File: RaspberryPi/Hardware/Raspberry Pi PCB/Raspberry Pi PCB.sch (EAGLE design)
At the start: 1 part

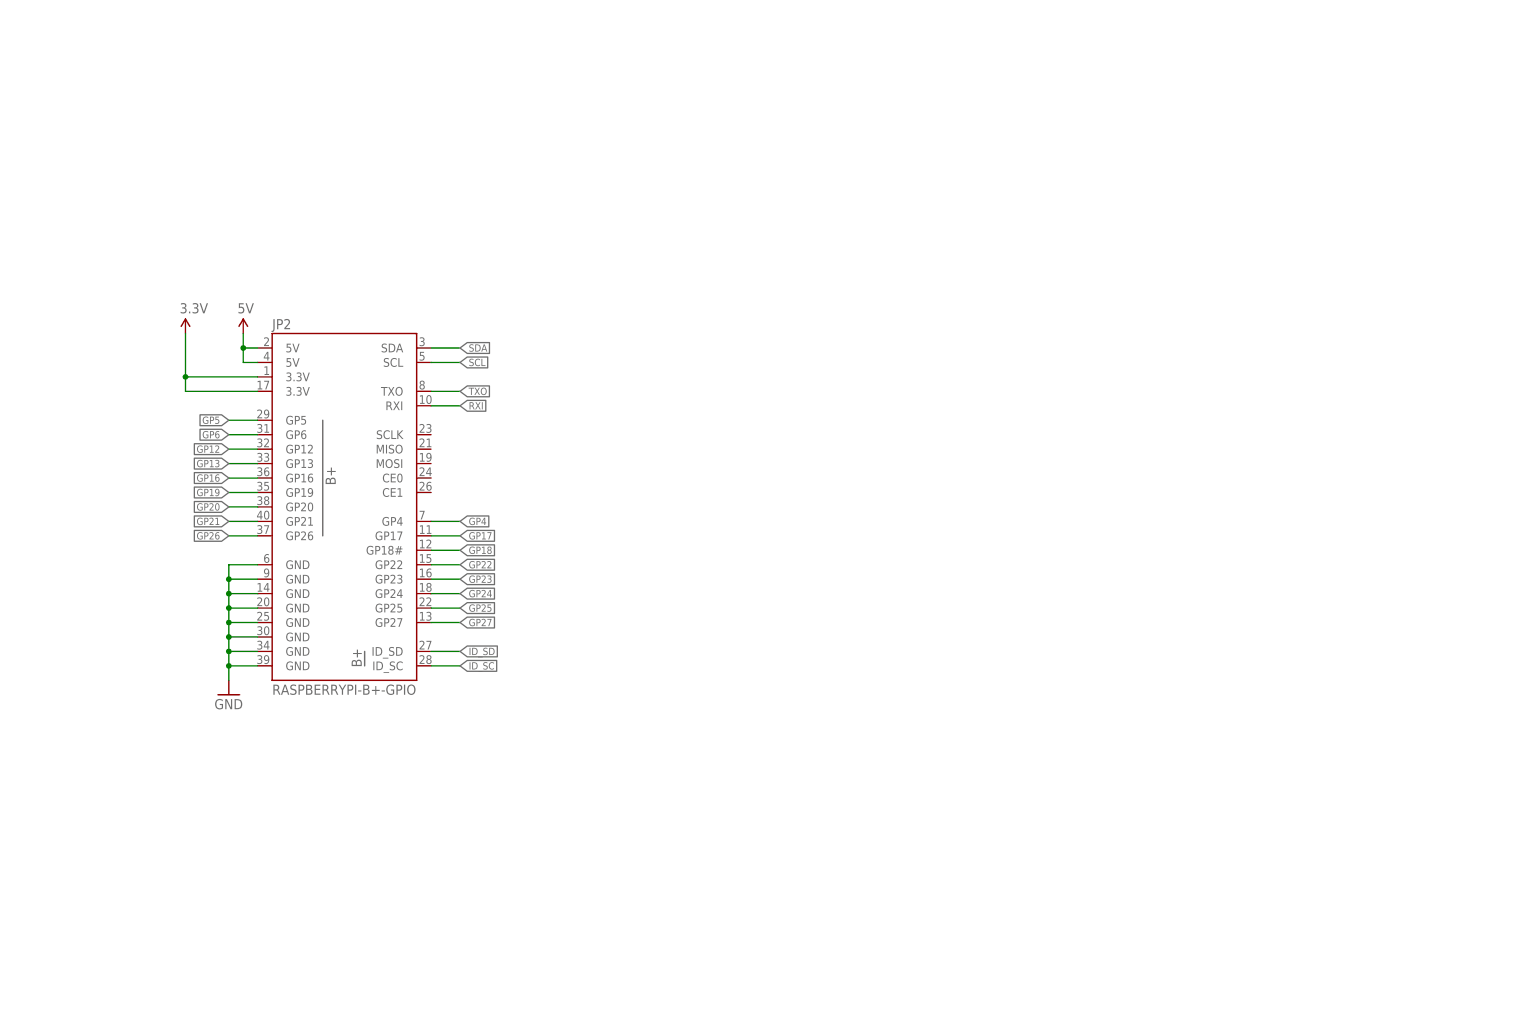
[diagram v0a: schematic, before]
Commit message: Added some necessary components for powering the Raspberry.
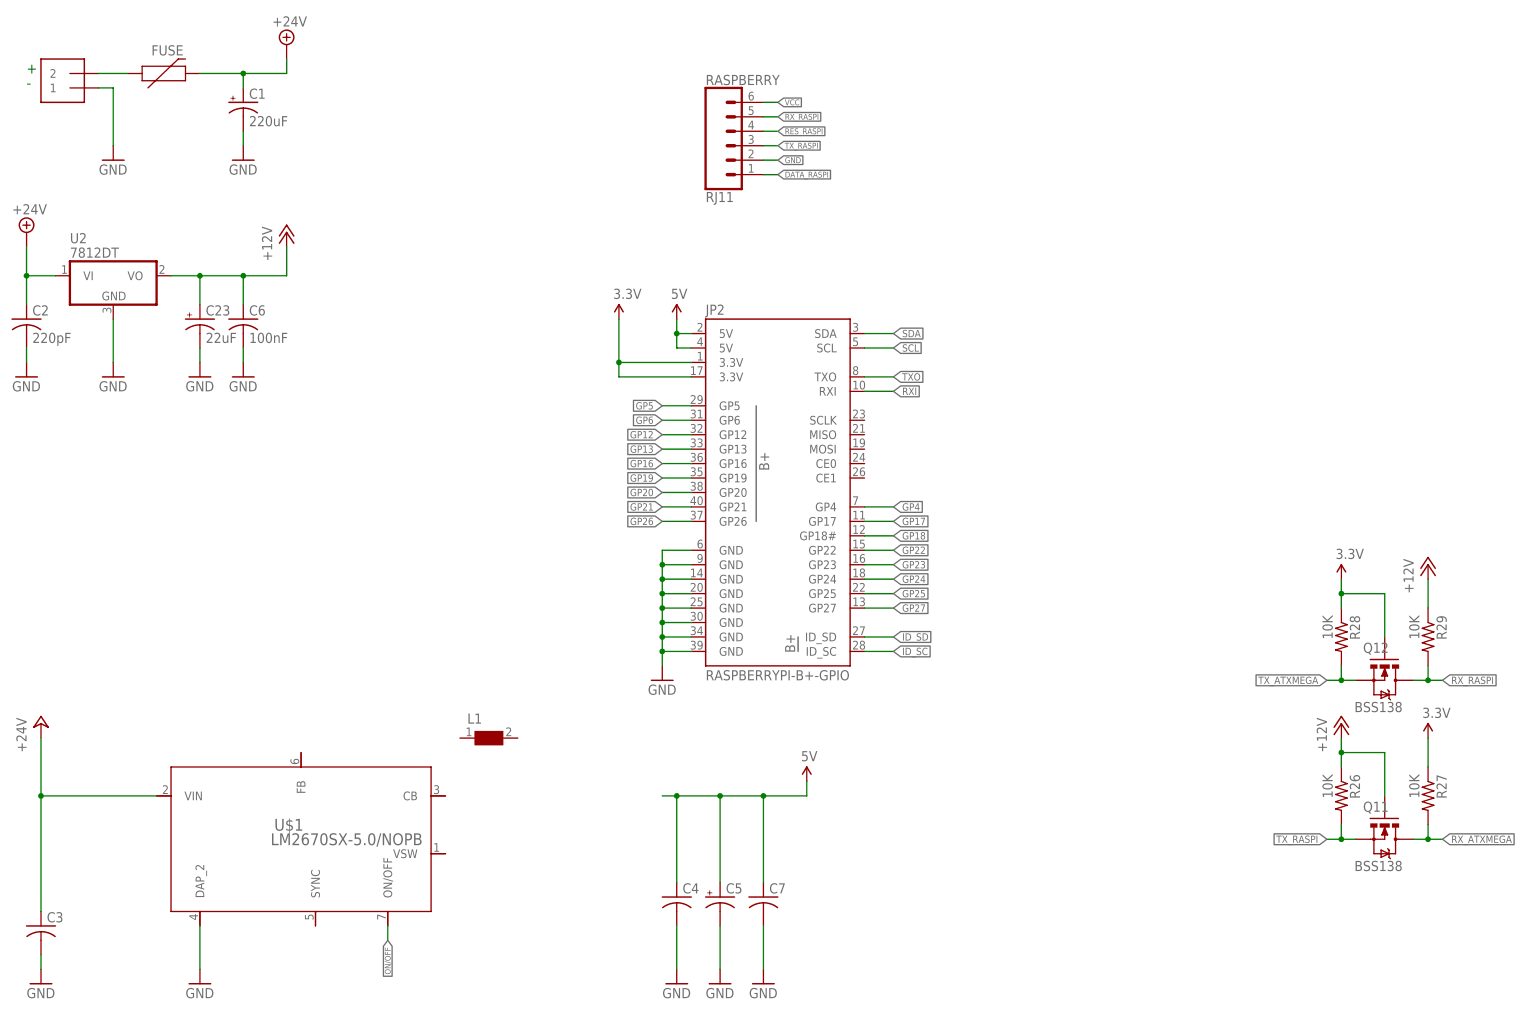
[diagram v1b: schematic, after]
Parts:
- added C1: 220uF, adafruit:CPOL-US175TMP-0810
- added C2: 220pF, adafruit:C-USC1206
- added C23: 22uF, adafruit:CPOL-US153CLV-0505
- added C3: (no value), adafruit:C-USC1206
- added C4, C7: (no value), adafruit:C-USC0805
- added C5: (no value), adafruit:CPOL-US153CLV-0505
- added C6: 100nF, adafruit:C-USC0805
- added FUSE: 6V/0.5A, SparkFun-Fuses:PPTC_HALF-AMP
- added J1: 1X2-3.5MM, adafruit:1X2-3.5MM
- added L1: (no value), WE-PD:WE-PD-7447709330_1260/1245/1280/1210
- added Q11, Q12: BSS138, SparkFun:MOSFET-NCHANNELSMD
- added R26, R27, R28, R29: 10K, SparkFun:RESISTOR0603-RES
- added RASPBERRY: RJ11, SparkFun-Connectors:RJ11-6
- added U$1: LM2670SX-5.0/NOPB, LM2670:LM2670SX-5.0/NOPB
- added U2: 7812DT, adafruit:7812DT
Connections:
- new net +12V: C23.+, C6.1, Q11.G, R26.1, R29.1, U2.VO
- new net +24V: C1.+, C2.1, C3.1, FUSE.2, U$1.VIN, U2.VI
- new net DATA_RASPI: RASPBERRY.1
- new net ON/OFF: U$1.ON/OFF
- new net RES_RASPI: RASPBERRY.4
- new net RX_ATXMEGA: Q11.D, R27.2
- new net RX_RASPI: Q12.D, R29.2, RASPBERRY.5
- new net TX_ATXMEGA: Q12.S, R28.2
- new net TX_RASPI: Q11.S, R26.2, RASPBERRY.3
- new net VCC: RASPBERRY.6
- new net VIN: FUSE.1, J1.2
- net 3.3V: now also Q12.G, R27.1, R28.1
- net 5V: now also C4.1, C5.+, C7.1
- net GND: now also C1.-, C2.2, C23.-, C3.2, C4.2, C5.-, C6.2, C7.2, J1.1, RASPBERRY.2, U$1.DAP_2, U2.GND
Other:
- note added: "+"
- note added: "-"
- moved on the sheet: JP2

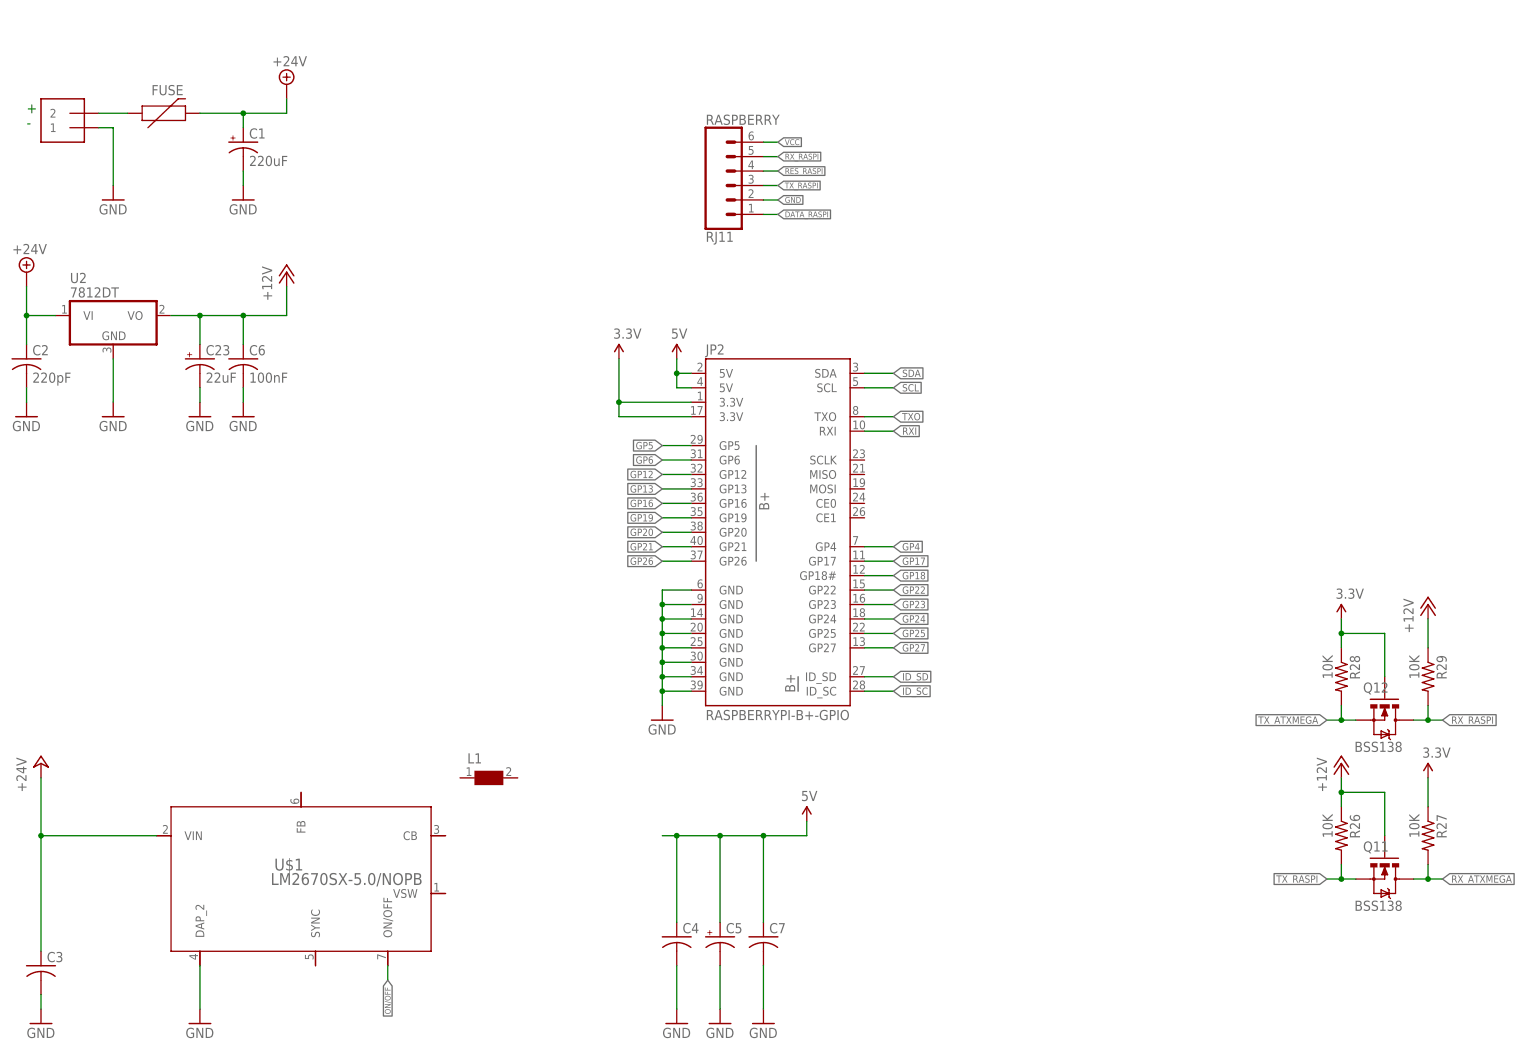
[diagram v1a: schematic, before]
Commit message: Power component changes.
The planned buck converter will not be used on the PCB. It was decided that an AC/DC converter will be used that was available from the first Bidon dispenser project. This converter already outputs the desired 5V with a sufficient current.
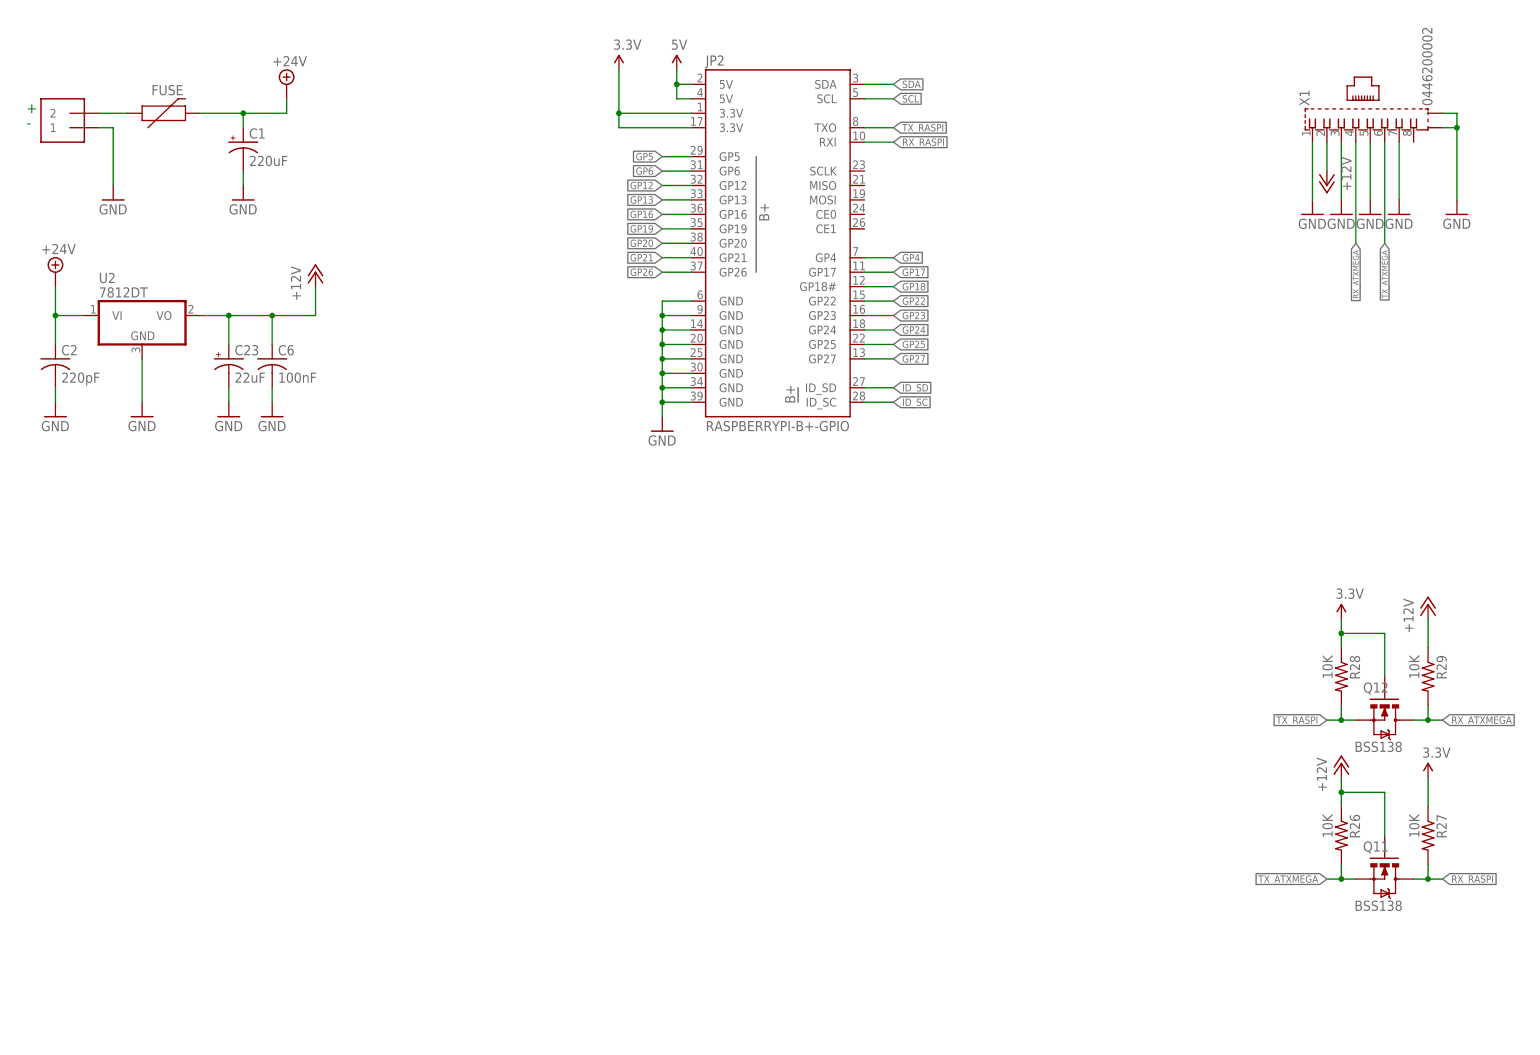
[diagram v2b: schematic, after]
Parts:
- removed C3: (no value), adafruit:C-USC1206
- removed C4, C7: (no value), adafruit:C-USC0805
- removed C5: (no value), adafruit:CPOL-US153CLV-0505
- removed L1: (no value), WE-PD:WE-PD-7447709330_1260/1245/1280/1210
- removed RASPBERRY: RJ11, SparkFun-Connectors:RJ11-6
- removed U$1: LM2670SX-5.0/NOPB, LM2670:LM2670SX-5.0/NOPB
- added X1: 0446200002, con-molex:0446200002
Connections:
- removed net DATA_RASPI: RASPBERRY.1
- removed net ON/OFF: U$1.ON/OFF
- removed net RES_RASPI: RASPBERRY.4
- removed net RXI: JP2.RXI
- removed net TXO: JP2.TXO
- removed net VCC: RASPBERRY.6
- net +12V: now also X1.2
- net +24V: no longer C3.1, U$1.VIN
- net 5V: no longer C4.1, C5.+, C7.1
- net GND: now also X1.1, X1.3, X1.5, X1.7, X1.S1, X1.S2; no longer C3.2, C4.2, C5.-, C7.2, RASPBERRY.2, U$1.DAP_2
- net RX_ATXMEGA: now also Q12.D, R29.2, X1.4; no longer Q11.D, R27.2
- net RX_RASPI: now also JP2.RXI, Q11.D, R27.2; no longer Q12.D, R29.2, RASPBERRY.5
- net TX_ATXMEGA: now also Q11.S, R26.2, X1.6; no longer Q12.S, R28.2
- net TX_RASPI: now also JP2.TXO, Q12.S, R28.2; no longer Q11.S, R26.2, RASPBERRY.3
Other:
- moved on the sheet: C2, C23, C6, JP2, U2

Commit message: Added a step up converter.
This step up is required for the 12 volt data communication between the Raspberry and the microcontroller. It ofcourse also works with the lower 5 volt, but for reliability we use 12 volt.
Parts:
- removed C23: 22uF, adafruit:CPOL-US153CLV-0505
- removed FUSE: 6V/0.5A, SparkFun-Fuses:PPTC_HALF-AMP
- removed J1: 1X2-3.5MM, adafruit:1X2-3.5MM
- removed U2: 7812DT, adafruit:7812DT
- added C10, C3, C4, C9: 100nF, SparkFun-Capacitors:1.0UF-0805-25V-(+80/-20%)
- added C5, C8: 10uF, adafruit:CPOL-US153CLV-0505
- added C7: (no value), adafruit:C-USC1206
- added D1: (no value), adafruit:DIODESOD-123
- added FUSE1: 6V/0.5A, SparkFun-Fuses:PPTC_HALF-AMP
- added J2: 1X2-3.5MM, adafruit:1X2-3.5MM
- added L1: CDRH4D18, inductor-sumida:CDRH4D18
- added P1: 87520-0010BLF, 87520-0010BLF:87520-0010BLF
- added R1, R2, R3: (no value), SparkFun-Resistors:RESISTOR0805
- added U1: TPS61040QDBVRQ1, Texas Instruments_By_element14_Batch_1:TPS61040QDBVRQ1
- C1: value 220uF -> 100uF
- C2: value 220pF -> 100uF; device adafruit:C-USC1206 -> adafruit:CPOL-US175TMP-0810
- C6: value 100nF -> 10uF; device adafruit:C-USC0805 -> adafruit:CPOL-US153CLV-0505
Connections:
- removed net +24V: C1.+, C2.1, FUSE.2, U2.VI
- removed net VIN: FUSE.1, J1.2
- new net +5V: C1.+, C2.+, C3.1, C4.1, C5.+, C6.+, FUSE1.2, L1.1, U1.EN, U1.VIN
- new net FEEDBACK: C7.2, R1.1, R2.2, U1.FB
- new net N$1: D1.A, L1.2, U1.SW
- new net N$2: R2.1, R3.2
- new net VIN1: FUSE1.1, J2.2
- net +12V: now also C7.1, C8.+, C9.1, D1.C, R1.2; no longer C23.+, C6.1, U2.VO
- net 5V: now also C10.1, P1.VCC
- net GND: now also C10.2, C2.-, C3.2, C4.2, C5.-, C6.-, C8.-, C9.2, J2.1, P1.GND, R3.1, U1.GND; no longer C2.2, C23.-, C6.2, J1.1, U2.GND
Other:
- note added: "5V input power"
